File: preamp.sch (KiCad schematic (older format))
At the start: 1 part

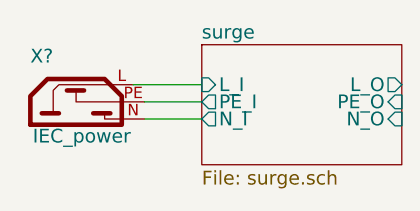
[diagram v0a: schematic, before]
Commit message: surge protection from ac net
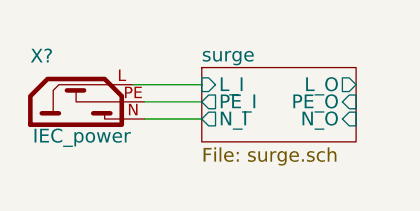
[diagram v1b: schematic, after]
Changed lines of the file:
@@
 LIBS:valves
 LIBS:selfmade
+LIBS:preamp-cache
 EELAYER 25 0
 EELAYER END
@@
 $EndDescr
 $Sheet
-S 1425 725  875  525
+S 1425 825  675  325
 U 5882A13F
 F0 "surge" 60
@@
 F3 "PE_I" O L 1425 975 60
 F4 "N_I" O L 1425 1050 60
-F5 "L_O" O R 2300 900 60
-F6 "PE_O" I R 2300 975 60
-F7 "N_O" I R 2300 1050 60
+F5 "L_O" O R 2100 900 60
+F6 "PE_O" I R 2100 975 60
+F7 "N_O" I R 2100 1050 60
 $EndSheet
 $Comp

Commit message: polarity_protection
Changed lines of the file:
@@
 EELAYER 25 0
 EELAYER END
-$Descr A3 16535 11693
+$Descr A4 11693 8268
 encoding utf-8
-Sheet 1 2
+Sheet 1 3
 Title ""
 Date ""
@@
 Wire Wire Line
 	1175 1050 1425 1050
+$Sheet
+S 2400 825  775  325
+U 58836B99
+F0 "polarity_protection" 60
+F1 "polarity_protection.sch" 60
+F2 "L_I" I L 2400 900 60
+F3 "PE_I" O L 2400 975 60
+F4 "N_I" O L 2400 1050 60
+F5 "L_O" O R 3175 900 60
+F6 "PE_O" I R 3175 975 60
+F7 "N_O" I R 3175 1050 60
+$EndSheet
+Wire Wire Line
+	2100 900  2400 900
+Wire Wire Line
+	2400 975  2100 975
+Wire Wire Line
+	2100 1050 2400 1050
 $EndSCHEMATC

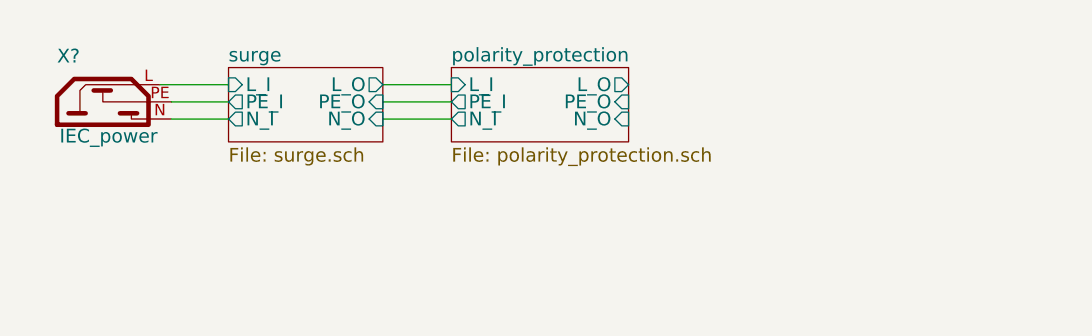
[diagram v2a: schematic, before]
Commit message: added relayboard and virtual case
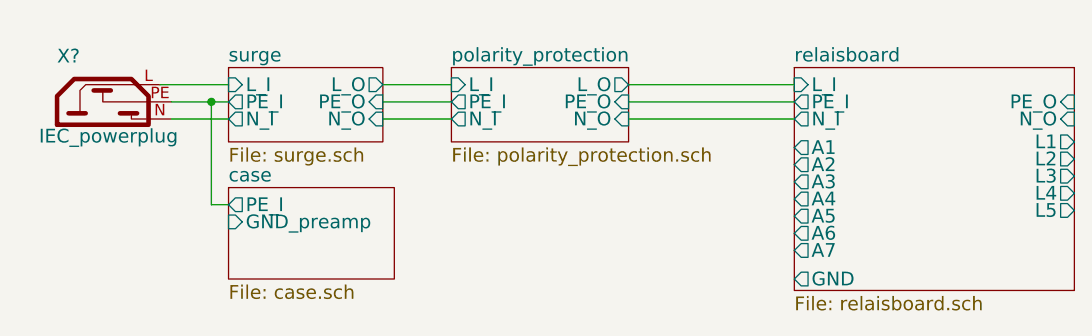
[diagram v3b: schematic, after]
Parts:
- X?: value IEC_power -> IEC_powerplug
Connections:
- net surge/PE_I renamed case/PE_I
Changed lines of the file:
@@
 $Descr A4 11693 8268
 encoding utf-8
-Sheet 1 3
+Sheet 1 5
 Title ""
 Date ""
@@
 P 675 1075
 F 0 "X?" H 725 1375 60  0000 C CNN
-F 1 "IEC_power" H 900 1025 60  0000 C CNN
+F 1 "IEC_powerplug" H 900 1025 60  0000 C CNN
 F 2 "" H 675 1075 60  0001 C CNN
 F 3 "" H 675 1075 60  0001 C CNN
@@
 Wire Wire Line
 	2100 1050 2400 1050
+$Sheet
+S 3900 825  1225 975
+U 58838AD0
+F0 "relaisboard" 60
+F1 "relaisboard.sch" 60
+F2 "L_I" I L 3900 900 60
+F3 "PE_I" O L 3900 975 60
+F4 "N_I" O L 3900 1050 60
+F5 "PE_O" I R 5125 975 60
+F6 "N_O" I R 5125 1050 60
+F7 "L1" O R 5125 1150 60
+F8 "L2" O R 5125 1225 60
+F9 "L3" O R 5125 1300 60
+F10 "L4" O R 5125 1375 60
+F11 "L5" O R 5125 1450 60
+F12 "GND" O L 3900 1750 60
+F13 "A1" O L 3900 1175 60
+F14 "A2" O L 3900 1250 60
+F15 "A3" O L 3900 1325 60
+F16 "A4" O L 3900 1400 60
+F17 "A5" O L 3900 1475 60
+F18 "A6" O L 3900 1550 60
+F19 "A7" O L 3900 1625 60
+$EndSheet
+Wire Wire Line
+	3900 900  3175 900
+Wire Wire Line
+	3175 975  3900 975
+Wire Wire Line
+	3900 1050 3175 1050
+$Sheet
+S 1425 1350 725  400
+U 5883E969
+F0 "case" 60
+F1 "case.sch" 60
+F2 "GND_preamp" I L 1425 1500 60
+F3 "PE_I" O L 1425 1425 60
+$EndSheet
+Wire Wire Line
+	1425 1425 1350 1425
+Wire Wire Line
+	1350 1425 1350 975
+Connection ~ 1350 975
 $EndSCHEMATC
